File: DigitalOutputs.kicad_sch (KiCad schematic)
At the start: 2 parts, among them J12 DIGITAL_OUTPUTS

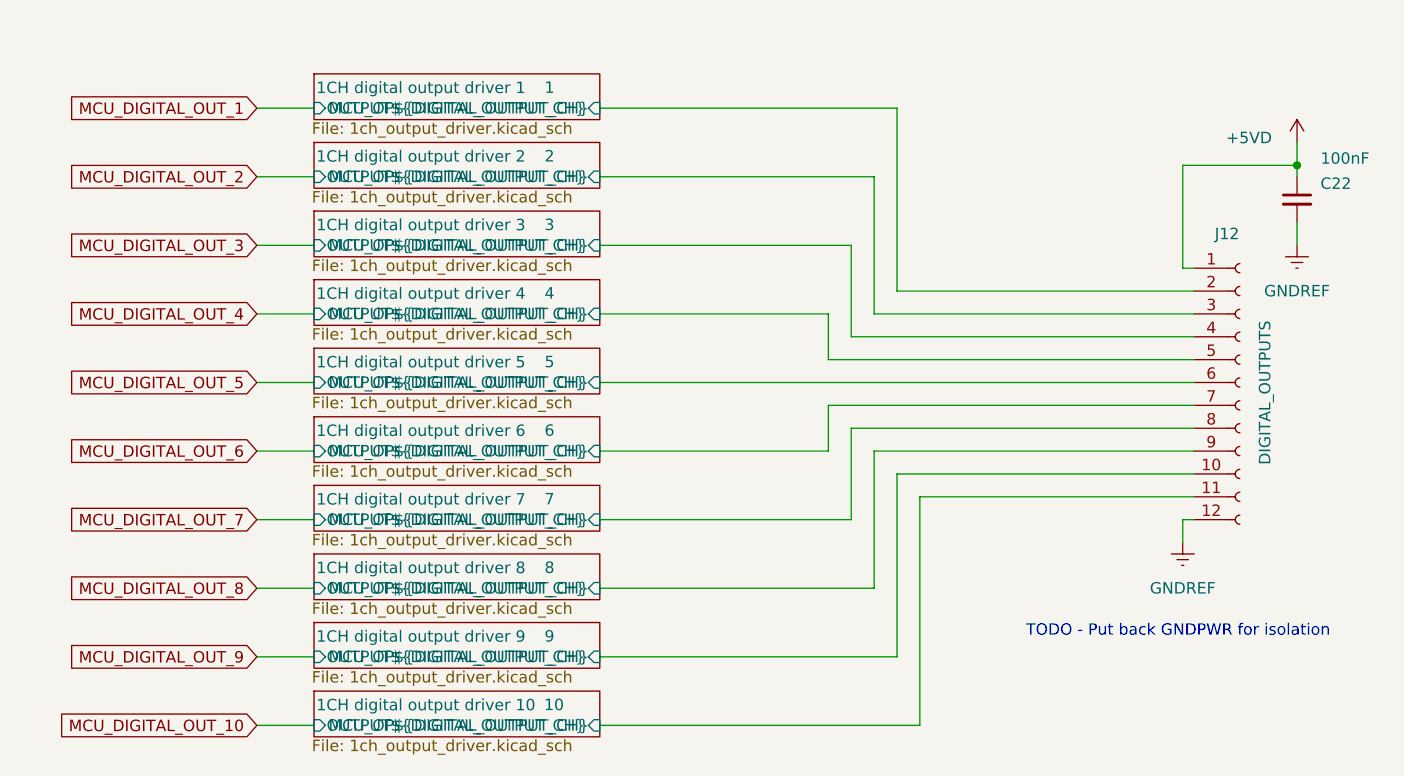
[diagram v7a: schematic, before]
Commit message: Dropped number of IO on design to make more room. Created the new footprints to suit them, updates to BOM and ran some traces on the PCB.
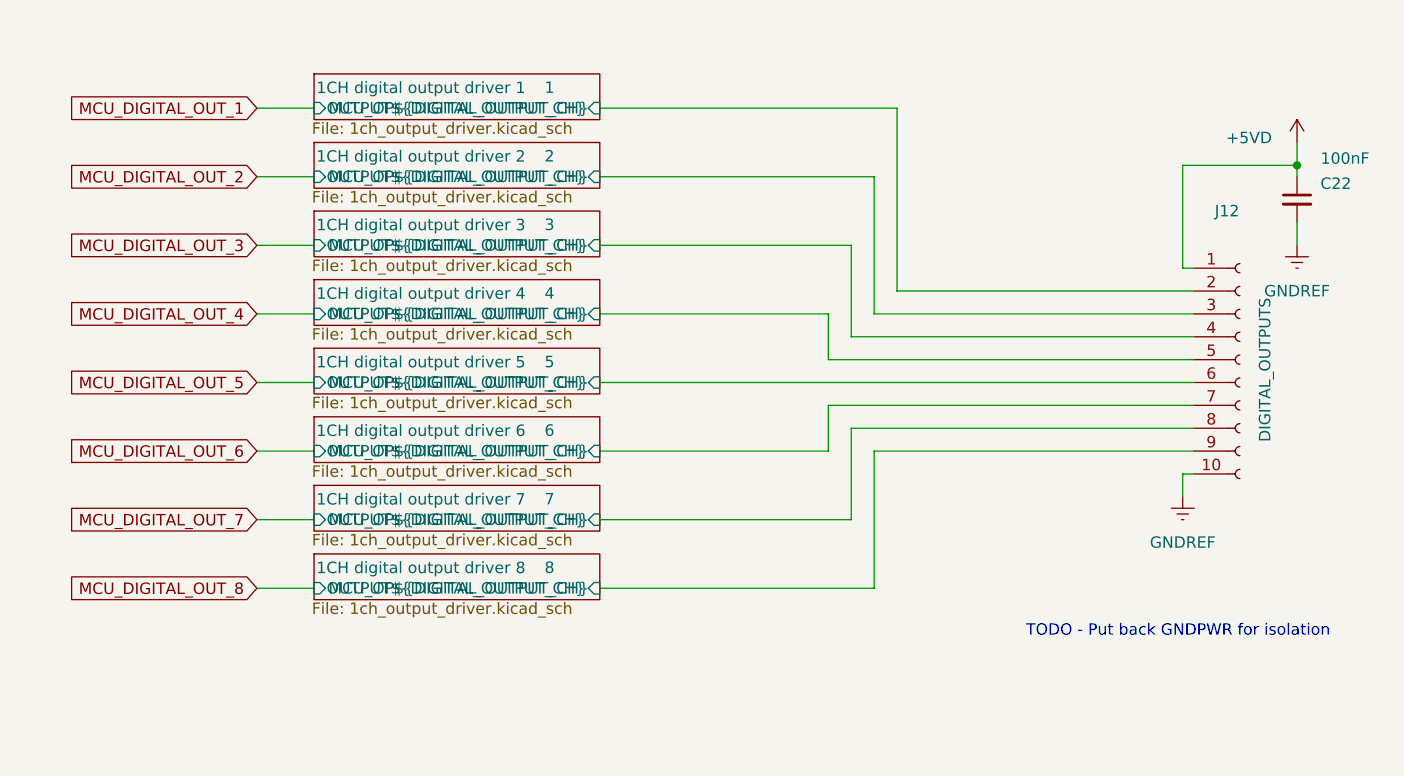
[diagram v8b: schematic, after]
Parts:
- J12: footprint EBWA_06_A:CONN_EBWA-12-A_ADM -> EBWA_06_A:CONN_EBWA-10-A_ADM; symbol Connector:Conn_01x12_Socket -> Connector:Conn_01x10_Socket
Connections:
- net 1CH digital output driver 9/OUTPUT${DIGITAL_OUTPUT_CH} is gone; now on net GNDREF: J12.10 (Pin_10)
- net GNDREF: no longer J12.12 (Pin_12)
- removed net 1CH digital output driver 10/OUTPUT${DIGITAL_OUTPUT_CH}: J12.11 (Pin_11)
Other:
- removed sheet 1CH digital output driver 10
- removed sheet 1CH digital output driver 9
